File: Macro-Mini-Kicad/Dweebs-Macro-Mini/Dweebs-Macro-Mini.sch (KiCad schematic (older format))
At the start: 57 parts, among them U1 ProMicro

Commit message: remade vias
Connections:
- net COL0: no longer U1.20 (F4)
- net COL1: no longer U1.7 (D4)
- net COL2: no longer U1.8 (C6)
- net COL3: no longer U1.9 (D7)
- net COL4: no longer U1.10 (E6)
- net COL5: no longer U1.11 (B4)
- net COL6: no longer U1.12 (B5)
- net ROW1: no longer U1.18 (F6)
- net ROW2: no longer U1.17 (F7)
- net ROW3: no longer U1.16 (B1)
- net ROW4: no longer U1.15 (B3)
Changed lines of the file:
@@
 $EndDescr
-$Comp
-L promicro:ProMicro U1
-U 1 1 622EFC0F
-P 2000 3400
-F 0 "U1" H 2000 4543 60  0000 C CNN
-F 1 "ProMicro" H 2000 4437 60  0000 C CNN
-F 2 "promicro:ProMicro" H 2000 4331 60  0000 C CNN
-F 3 "" H 2100 2350 60  0000 C CNN
-	1    2000 3400
-	1    0    0    -1
-$EndComp
 $Comp
 L MX_Alps_Hybrid:MX-NoLED MX1
@@
 Text GLabel 7350 1350 1    50   Input ~ 0
 COL6
+Wire Wire Line
+	4950 1800 4950 1350
+Wire Wire Line
+	5350 1800 5350 1350
+Wire Wire Line
+	5750 1800 5750 1350
+Wire Wire Line
+	6150 1800 6150 1350
+Wire Wire Line
+	6550 1800 6550 1350
+Wire Wire Line
+	6950 1800 6950 1350
+Wire Wire Line
+	7350 1800 7350 1350
+Wire Wire Line
+	4650 4850 4300 4850
+Wire Wire Line
+	4650 4200 4300 4200
+Wire Wire Line
+	4650 3550 4300 3550
+Wire Wire Line
+	4650 2850 4300 2850
 NoConn ~ 2300 2700
+$Comp
+L promicro:ProMicro U1
+U 1 1 622EFC0F
+P 2000 3400
+F 0 "U1" H 2000 4543 60  0000 C CNN
+F 1 "ProMicro" H 2000 4437 60  0000 C CNN
+F 2 "promicro:ProMicro" H 2000 4331 60  0000 C CNN
+F 3 "" H 2100 2350 60  0000 C CNN
+	1    2000 3400
+	1    0    0    -1
+$EndComp
+Wire Wire Line
+	3000 2200 3000 3150
+Wire Wire Line
+	3000 3150 2700 3150
 Wire Wire Line
 	3000 2200 4650 2200
-Wire Wire Line
-	3100 2850 4650 2850
-Wire Wire Line
-	3800 3250 3800 3550
-Wire Wire Line
-	3800 3550 4650 3550
-Wire Wire Line
-	3600 3350 3600 4200
-Wire Wire Line
-	3600 4200 4650 4200
-Wire Wire Line
-	3450 4850 4650 4850
-Wire Wire Line
-	7350 750  600  750
-Wire Wire Line
-	600  750  600  3750
-Wire Wire Line
-	600  3750 1300 3750
-Wire Wire Line
-	7350 750  7350 1800
-Wire Wire Line
-	6950 800  700  800
-Wire Wire Line
-	700  800  700  3650
-Wire Wire Line
-	700  3650 1300 3650
-Wire Wire Line
-	6950 800  6950 1800
-Wire Wire Line
-	6550 850  750  850
-Wire Wire Line
-	750  850  750  3550
-Wire Wire Line
-	750  3550 1300 3550
-Wire Wire Line
-	6550 850  6550 1800
-Wire Wire Line
-	6150 900  800  900
-Wire Wire Line
-	800  900  800  3450
-Wire Wire Line
-	800  3450 1300 3450
-Wire Wire Line
-	6150 900  6150 1800
-Wire Wire Line
-	5750 950  850  950
-Wire Wire Line
-	850  950  850  3350
-Wire Wire Line
-	850  3350 1300 3350
-Wire Wire Line
-	5750 950  5750 1800
-Wire Wire Line
-	5350 1000 900  1000
-Wire Wire Line
-	900  1000 900  3250
-Wire Wire Line
-	900  3250 1300 3250
-Wire Wire Line
-	5350 1000 5350 1800
-Wire Wire Line
-	4950 1050 2850 1050
-Wire Wire Line
-	4950 1050 4950 1800
-Wire Wire Line
-	2850 1050 2850 3050
-Wire Wire Line
-	2850 3050 2700 3050
-Wire Wire Line
-	3000 3150 2700 3150
-Wire Wire Line
-	3000 2200 3000 3150
-Wire Wire Line
-	3100 3250 2700 3250
-Wire Wire Line
-	3100 2850 3100 3250
-Wire Wire Line
-	3800 3250 3150 3250
-Wire Wire Line
-	3150 3250 3150 3350
-Wire Wire Line
-	3150 3350 2700 3350
-Wire Wire Line
-	3600 3350 3250 3350
-Wire Wire Line
-	3250 3350 3250 3450
-Wire Wire Line
-	3250 3450 2700 3450
-Wire Wire Line
-	3450 3550 2700 3550
-Wire Wire Line
-	3450 3550 3450 4850
 $EndSCHEMATC

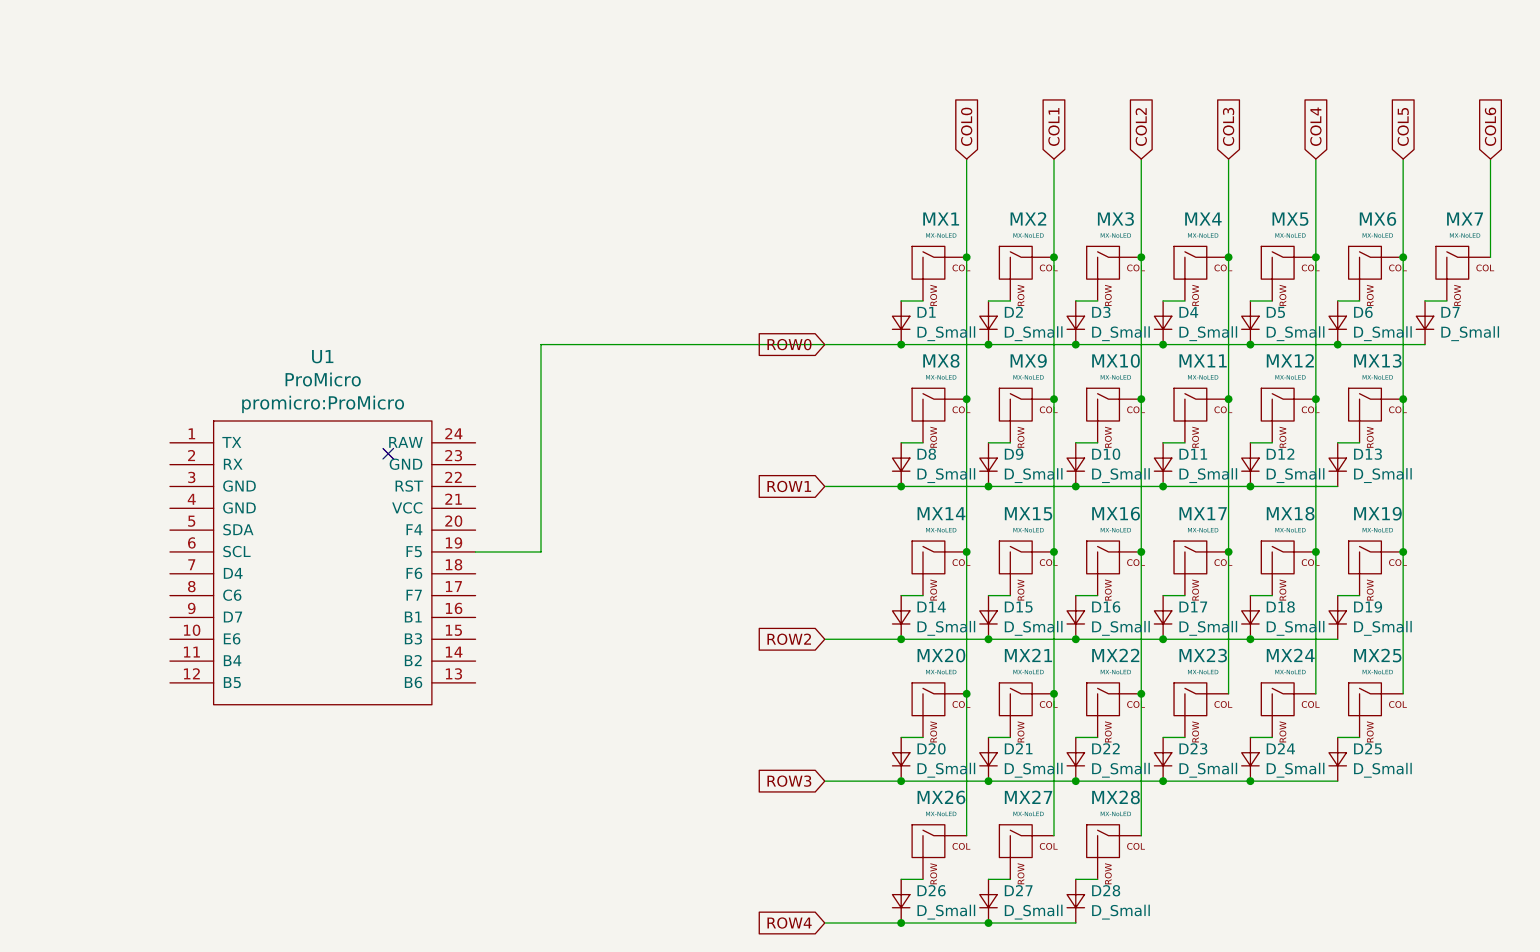
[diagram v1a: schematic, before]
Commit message: trace reroute
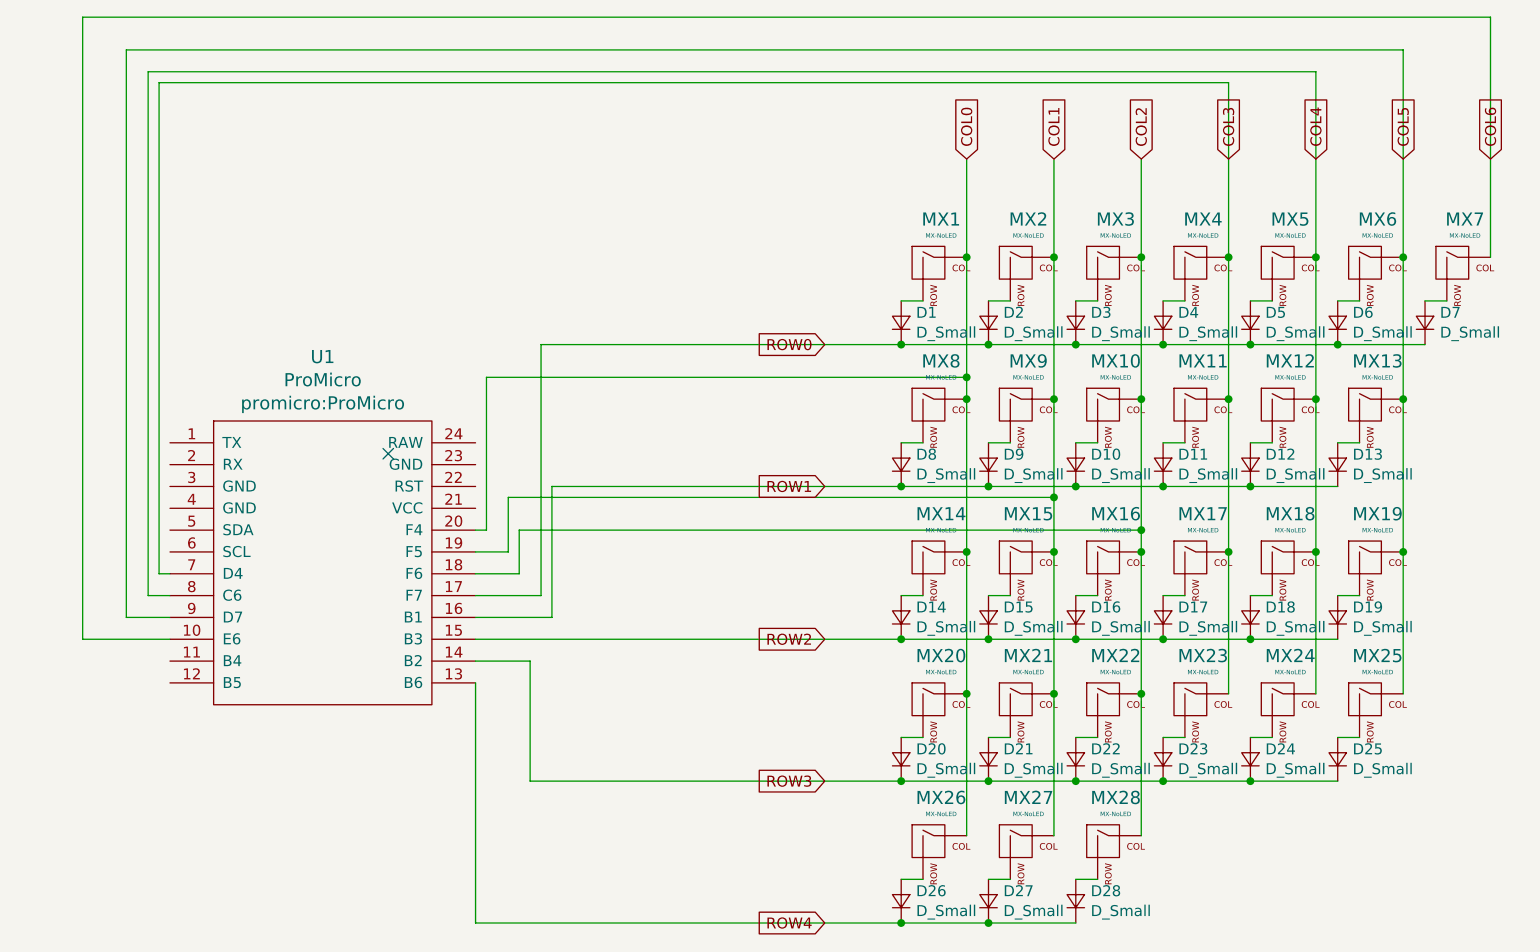
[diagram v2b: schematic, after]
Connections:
- net COL0: now also U1.20 (F4)
- net COL1: now also U1.19 (F5)
- net COL2: now also U1.18 (F6)
- net COL3: now also U1.7 (D4)
- net COL4: now also U1.8 (C6)
- net COL5: now also U1.9 (D7)
- net COL6: now also U1.10 (E6)
- net ROW0: now also U1.17 (F7); no longer U1.19 (F5)
- net ROW1: now also U1.16 (B1)
- net ROW2: now also U1.15 (B3)
- net ROW3: now also U1.14 (B2)
- net ROW4: now also U1.13 (B6)
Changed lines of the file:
@@
 Connection ~ 4950 3150
 Wire Wire Line
-	4950 2450 4950 1800
+	4950 2450 4950 2350
 Connection ~ 4950 2450
 Connection ~ 4950 1800
@@
 Connection ~ 5350 3800
 Wire Wire Line
-	5350 3150 5350 2450
+	5350 3150 5350 2900
 Connection ~ 5350 3150
 Wire Wire Line
@@
 	5750 3800 5750 3150
 Wire Wire Line
-	5750 3150 5750 2450
+	5750 3150 5750 3050
 Connection ~ 5750 3150
 Wire Wire Line
@@
 	4950 1800 4950 1350
 Wire Wire Line
-	5350 1800 5350 1350
-Wire Wire Line
 	5750 1800 5750 1350
-Wire Wire Line
-	6150 1800 6150 1350
-Wire Wire Line
-	6550 1800 6550 1350
-Wire Wire Line
-	6950 1800 6950 1350
-Wire Wire Line
-	7350 1800 7350 1350
-Wire Wire Line
-	4650 4850 4300 4850
-Wire Wire Line
-	4650 4200 4300 4200
-Wire Wire Line
-	4650 3550 4300 3550
-Wire Wire Line
-	4650 2850 4300 2850
 NoConn ~ 2300 2700
 $Comp
@@
 $EndComp
 Wire Wire Line
-	3000 2200 3000 3150
+	3000 2200 4650 2200
 Wire Wire Line
-	3000 3150 2700 3150
+	3050 2850 4650 2850
 Wire Wire Line
-	3000 2200 4650 2200
+	2950 4200 4650 4200
+Wire Wire Line
+	2700 4850 2700 3750
+Wire Wire Line
+	2700 4850 4650 4850
+Wire Wire Line
+	2950 4200 2950 3650
+Wire Wire Line
+	2950 3650 2700 3650
+Wire Wire Line
+	2700 3550 4650 3550
+Wire Wire Line
+	3050 2850 3050 3450
+Wire Wire Line
+	3050 3450 2700 3450
+Wire Wire Line
+	3000 2200 3000 3350
+Wire Wire Line
+	3000 3350 2700 3350
+Wire Wire Line
+	5350 1800 5350 1350
+Wire Wire Line
+	5750 3050 2900 3050
+Wire Wire Line
+	2900 3050 2900 3250
+Wire Wire Line
+	2900 3250 2700 3250
+Connection ~ 5750 3050
+Wire Wire Line
+	5750 3050 5750 2450
+Wire Wire Line
+	5350 2900 2850 2900
+Wire Wire Line
+	2850 2900 2850 3150
+Wire Wire Line
+	2850 3150 2700 3150
+Connection ~ 5350 2900
+Wire Wire Line
+	5350 2900 5350 2450
+Wire Wire Line
+	4950 2350 2750 2350
+Wire Wire Line
+	2750 2350 2750 3050
+Wire Wire Line
+	2750 3050 2700 3050
+Connection ~ 4950 2350
+Wire Wire Line
+	4950 2350 4950 1800
+Wire Wire Line
+	6150 1000 1250 1000
+Wire Wire Line
+	1250 1000 1250 3250
+Wire Wire Line
+	1250 3250 1300 3250
+Wire Wire Line
+	6150 1000 6150 1800
+Wire Wire Line
+	6550 950  1200 950
+Wire Wire Line
+	1200 950  1200 3350
+Wire Wire Line
+	1200 3350 1300 3350
+Wire Wire Line
+	6550 950  6550 1800
+Wire Wire Line
+	6950 850  1100 850
+Wire Wire Line
+	1100 850  1100 3450
+Wire Wire Line
+	1100 3450 1300 3450
+Wire Wire Line
+	6950 850  6950 1800
+Wire Wire Line
+	7350 700  900  700
+Wire Wire Line
+	900  700  900  3550
+Wire Wire Line
+	900  3550 1300 3550
+Wire Wire Line
+	7350 700  7350 1800
 $EndSCHEMATC

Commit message: more crap
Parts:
- MX1, MX10, MX11, MX12, MX13, MX14, MX15, MX16, MX17, MX18, MX19, MX2, MX20, MX21, MX22, MX23, MX24, MX25, MX26, MX27, MX28, MX3, MX4, MX5, MX6, MX7, MX8, MX9: footprint MX_Alps_Hybrid:MX-1U-NoLED -> kbd:CherryMX_1u
- U1: footprint promicro:ProMicro -> other_parts:ProMicro
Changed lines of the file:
@@
 EESchema Schematic File Version 4
+LIBS:Dweebs-Macro-Mini-cache
 EELAYER 30 0
 EELAYER END
@@
 F 0 "MX1" H 4833 2073 60  0000 C CNN
 F 1 "MX-NoLED" H 4833 1999 20  0000 C CNN
-F 2 "MX_Alps_Hybrid:MX-1U-NoLED" H 4175 1825 60  0001 C CNN
+F 2 "kbd:CherryMX_1u" H 4175 1825 60  0001 C CNN
 F 3 "" H 4175 1825 60  0001 C CNN
 	1    4800 1850
@@
 F 0 "MX2" H 5233 2073 60  0000 C CNN
 F 1 "MX-NoLED" H 5233 1999 20  0000 C CNN
-F 2 "MX_Alps_Hybrid:MX-1U-NoLED" H 4575 1825 60  0001 C CNN
+F 2 "kbd:CherryMX_1u" H 4575 1825 60  0001 C CNN
 F 3 "" H 4575 1825 60  0001 C CNN
 	1    5200 1850
@@
 F 0 "MX3" H 5633 2073 60  0000 C CNN
 F 1 "MX-NoLED" H 5633 1999 20  0000 C CNN
-F 2 "MX_Alps_Hybrid:MX-1U-NoLED" H 4975 1825 60  0001 C CNN
+F 2 "kbd:CherryMX_1u" H 4975 1825 60  0001 C CNN
 F 3 "" H 4975 1825 60  0001 C CNN
 	1    5600 1850
@@
 F 0 "MX4" H 6033 2073 60  0000 C CNN
 F 1 "MX-NoLED" H 6033 1999 20  0000 C CNN
-F 2 "MX_Alps_Hybrid:MX-1U-NoLED" H 5375 1825 60  0001 C CNN
+F 2 "kbd:CherryMX_1u" H 5375 1825 60  0001 C CNN
 F 3 "" H 5375 1825 60  0001 C CNN
 	1    6000 1850
@@
 F 0 "MX5" H 6433 2073 60  0000 C CNN
 F 1 "MX-NoLED" H 6433 1999 20  0000 C CNN
-F 2 "MX_Alps_Hybrid:MX-1U-NoLED" H 5775 1825 60  0001 C CNN
+F 2 "kbd:CherryMX_1u" H 5775 1825 60  0001 C CNN
 F 3 "" H 5775 1825 60  0001 C CNN
 	1    6400 1850
@@
 F 0 "MX6" H 6833 2073 60  0000 C CNN
 F 1 "MX-NoLED" H 6833 1999 20  0000 C CNN
-F 2 "MX_Alps_Hybrid:MX-1U-NoLED" H 6175 1825 60  0001 C CNN
+F 2 "kbd:CherryMX_1u" H 6175 1825 60  0001 C CNN
 F 3 "" H 6175 1825 60  0001 C CNN
 	1    6800 1850
@@
 F 0 "MX7" H 7233 2073 60  0000 C CNN
 F 1 "MX-NoLED" H 7233 1999 20  0000 C CNN
-F 2 "MX_Alps_Hybrid:MX-1U-NoLED" H 6575 1825 60  0001 C CNN
+F 2 "kbd:CherryMX_1u" H 6575 1825 60  0001 C CNN
 F 3 "" H 6575 1825 60  0001 C CNN
 	1    7200 1850
@@
 F 0 "MX8" H 4833 2723 60  0000 C CNN
 F 1 "MX-NoLED" H 4833 2649 20  0000 C CNN
-F 2 "MX_Alps_Hybrid:MX-1U-NoLED" H 4175 2475 60  0001 C CNN
+F 2 "kbd:CherryMX_1u" H 4175 2475 60  0001 C CNN
 F 3 "" H 4175 2475 60  0001 C CNN
 	1    4800 2500
@@
 F 0 "MX9" H 5233 2723 60  0000 C CNN
 F 1 "MX-NoLED" H 5233 2649 20  0000 C CNN
-F 2 "MX_Alps_Hybrid:MX-1U-NoLED" H 4575 2475 60  0001 C CNN
+F 2 "kbd:CherryMX_1u" H 4575 2475 60  0001 C CNN
 F 3 "" H 4575 2475 60  0001 C CNN
 	1    5200 2500
@@
 F 0 "MX10" H 5633 2723 60  0000 C CNN
 F 1 "MX-NoLED" H 5633 2649 20  0000 C CNN
-F 2 "MX_Alps_Hybrid:MX-1U-NoLED" H 4975 2475 60  0001 C CNN
+F 2 "kbd:CherryMX_1u" H 4975 2475 60  0001 C CNN
 F 3 "" H 4975 2475 60  0001 C CNN
 	1    5600 2500
@@
 F 0 "MX11" H 6033 2723 60  0000 C CNN
 F 1 "MX-NoLED" H 6033 2649 20  0000 C CNN
-F 2 "MX_Alps_Hybrid:MX-1U-NoLED" H 5375 2475 60  0001 C CNN
+F 2 "kbd:CherryMX_1u" H 5375 2475 60  0001 C CNN
 F 3 "" H 5375 2475 60  0001 C CNN
 	1    6000 2500
@@
 F 0 "MX12" H 6433 2723 60  0000 C CNN
 F 1 "MX-NoLED" H 6433 2649 20  0000 C CNN
-F 2 "MX_Alps_Hybrid:MX-1U-NoLED" H 5775 2475 60  0001 C CNN
+F 2 "kbd:CherryMX_1u" H 5775 2475 60  0001 C CNN
 F 3 "" H 5775 2475 60  0001 C CNN
 	1    6400 2500
@@
 F 0 "MX13" H 6833 2723 60  0000 C CNN
 F 1 "MX-NoLED" H 6833 2649 20  0000 C CNN
-F 2 "MX_Alps_Hybrid:MX-1U-NoLED" H 6175 2475 60  0001 C CNN
+F 2 "kbd:CherryMX_1u" H 6175 2475 60  0001 C CNN
 F 3 "" H 6175 2475 60  0001 C CNN
 	1    6800 2500
@@
 F 0 "MX14" H 4833 3423 60  0000 C CNN
 F 1 "MX-NoLED" H 4833 3349 20  0000 C CNN
-F 2 "MX_Alps_Hybrid:MX-1U-NoLED" H 4175 3175 60  0001 C CNN
+F 2 "kbd:CherryMX_1u" H 4175 3175 60  0001 C CNN
 F 3 "" H 4175 3175 60  0001 C CNN
 	1    4800 3200
@@
 F 0 "MX15" H 5233 3423 60  0000 C CNN
 F 1 "MX-NoLED" H 5233 3349 20  0000 C CNN
-F 2 "MX_Alps_Hybrid:MX-1U-NoLED" H 4575 3175 60  0001 C CNN
+F 2 "kbd:CherryMX_1u" H 4575 3175 60  0001 C CNN
 F 3 "" H 4575 3175 60  0001 C CNN
 	1    5200 3200
@@
 F 0 "MX16" H 5633 3423 60  0000 C CNN
 F 1 "MX-NoLED" H 5633 3349 20  0000 C CNN
-F 2 "MX_Alps_Hybrid:MX-1U-NoLED" H 4975 3175 60  0001 C CNN
+F 2 "kbd:CherryMX_1u" H 4975 3175 60  0001 C CNN
 F 3 "" H 4975 3175 60  0001 C CNN
 	1    5600 3200
@@
 F 0 "MX17" H 6033 3423 60  0000 C CNN
 F 1 "MX-NoLED" H 6033 3349 20  0000 C CNN
-F 2 "MX_Alps_Hybrid:MX-1U-NoLED" H 5375 3175 60  0001 C CNN
+F 2 "kbd:CherryMX_1u" H 5375 3175 60  0001 C CNN
 F 3 "" H 5375 3175 60  0001 C CNN
 	1    6000 3200
@@
 F 0 "MX18" H 6433 3423 60  0000 C CNN
 F 1 "MX-NoLED" H 6433 3349 20  0000 C CNN
-F 2 "MX_Alps_Hybrid:MX-1U-NoLED" H 5775 3175 60  0001 C CNN
+F 2 "kbd:CherryMX_1u" H 5775 3175 60  0001 C CNN
 F 3 "" H 5775 3175 60  0001 C CNN
 	1    6400 3200
@@
 F 0 "MX19" H 6833 3423 60  0000 C CNN
 F 1 "MX-NoLED" H 6833 3349 20  0000 C CNN
-F 2 "MX_Alps_Hybrid:MX-1U-NoLED" H 6175 3175 60  0001 C CNN
+F 2 "kbd:CherryMX_1u" H 6175 3175 60  0001 C CNN
 F 3 "" H 6175 3175 60  0001 C CNN
 	1    6800 3200
@@
 F 0 "MX20" H 4833 4073 60  0000 C CNN
 F 1 "MX-NoLED" H 4833 3999 20  0000 C CNN
-F 2 "MX_Alps_Hybrid:MX-1U-NoLED" H 4175 3825 60  0001 C CNN
+F 2 "kbd:CherryMX_1u" H 4175 3825 60  0001 C CNN
 F 3 "" H 4175 3825 60  0001 C CNN
 	1    4800 3850
@@
 F 0 "MX21" H 5233 4073 60  0000 C CNN
 F 1 "MX-NoLED" H 5233 3999 20  0000 C CNN
-F 2 "MX_Alps_Hybrid:MX-1U-NoLED" H 4575 3825 60  0001 C CNN
+F 2 "kbd:CherryMX_1u" H 4575 3825 60  0001 C CNN
 F 3 "" H 4575 3825 60  0001 C CNN
 	1    5200 3850
@@
 F 0 "MX22" H 5633 4073 60  0000 C CNN
 F 1 "MX-NoLED" H 5633 3999 20  0000 C CNN
-F 2 "MX_Alps_Hybrid:MX-1U-NoLED" H 4975 3825 60  0001 C CNN
+F 2 "kbd:CherryMX_1u" H 4975 3825 60  0001 C CNN
 F 3 "" H 4975 3825 60  0001 C CNN
 	1    5600 3850
@@
 F 0 "MX23" H 6033 4073 60  0000 C CNN
 F 1 "MX-NoLED" H 6033 3999 20  0000 C CNN
-F 2 "MX_Alps_Hybrid:MX-1U-NoLED" H 5375 3825 60  0001 C CNN
+F 2 "kbd:CherryMX_1u" H 5375 3825 60  0001 C CNN
 F 3 "" H 5375 3825 60  0001 C CNN
 	1    6000 3850
@@
 F 0 "MX24" H 6433 4073 60  0000 C CNN
 F 1 "MX-NoLED" H 6433 3999 20  0000 C CNN
-F 2 "MX_Alps_Hybrid:MX-1U-NoLED" H 5775 3825 60  0001 C CNN
+F 2 "kbd:CherryMX_1u" H 5775 3825 60  0001 C CNN
 F 3 "" H 5775 3825 60  0001 C CNN
 	1    6400 3850
@@
 F 0 "MX25" H 6833 4073 60  0000 C CNN
 F 1 "MX-NoLED" H 6833 3999 20  0000 C CNN
-F 2 "MX_Alps_Hybrid:MX-1U-NoLED" H 6175 3825 60  0001 C CNN
+F 2 "kbd:CherryMX_1u" H 6175 3825 60  0001 C CNN
 F 3 "" H 6175 3825 60  0001 C CNN
 	1    6800 3850
@@
 F 0 "MX26" H 4833 4723 60  0000 C CNN
 F 1 "MX-NoLED" H 4833 4649 20  0000 C CNN
-F 2 "MX_Alps_Hybrid:MX-1U-NoLED" H 4175 4475 60  0001 C CNN
+F 2 "kbd:CherryMX_1u" H 4175 4475 60  0001 C CNN
 F 3 "" H 4175 4475 60  0001 C CNN
 	1    4800 4500
@@
 F 0 "MX27" H 5233 4723 60  0000 C CNN
 F 1 "MX-NoLED" H 5233 4649 20  0000 C CNN
-F 2 "MX_Alps_Hybrid:MX-1U-NoLED" H 4575 4475 60  0001 C CNN
+F 2 "kbd:CherryMX_1u" H 4575 4475 60  0001 C CNN
 F 3 "" H 4575 4475 60  0001 C CNN
 	1    5200 4500
@@
 F 0 "MX28" H 5633 4723 60  0000 C CNN
 F 1 "MX-NoLED" H 5633 4649 20  0000 C CNN
-F 2 "MX_Alps_Hybrid:MX-1U-NoLED" H 4975 4475 60  0001 C CNN
+F 2 "kbd:CherryMX_1u" H 4975 4475 60  0001 C CNN
 F 3 "" H 4975 4475 60  0001 C CNN
 	1    5600 4500
@@
 F 0 "U1" H 2000 4543 60  0000 C CNN
 F 1 "ProMicro" H 2000 4437 60  0000 C CNN
-F 2 "promicro:ProMicro" H 2000 4331 60  0000 C CNN
+F 2 "other_parts:ProMicro" H 2000 4331 60  0000 C CNN
 F 3 "" H 2100 2350 60  0000 C CNN
 	1    2000 3400
